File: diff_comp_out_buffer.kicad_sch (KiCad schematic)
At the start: 7 parts, among them U1 TLV3601, U48 SN74LVC2G126

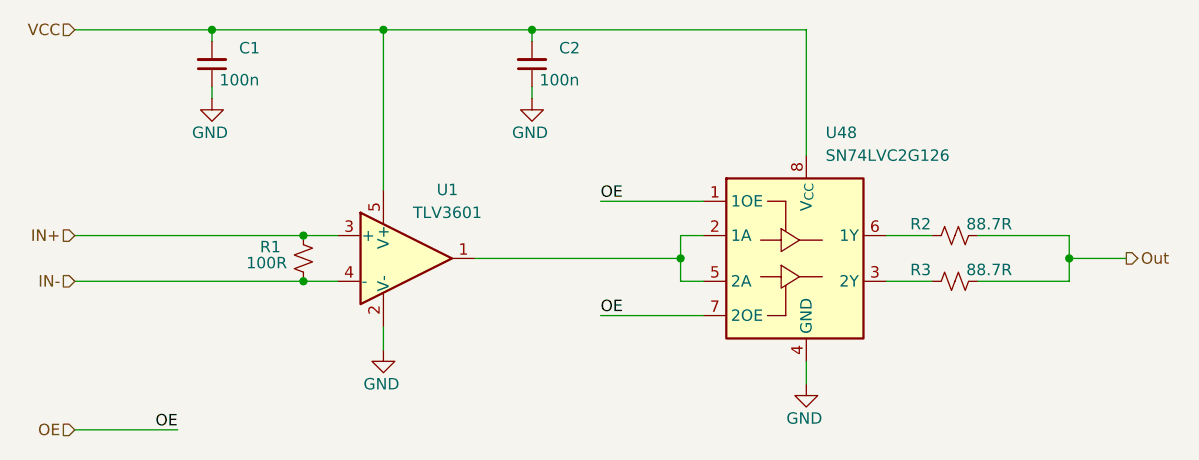
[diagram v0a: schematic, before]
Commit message: Fixed Silkscreen and BOM
All DRC/ERC errors are resolved.
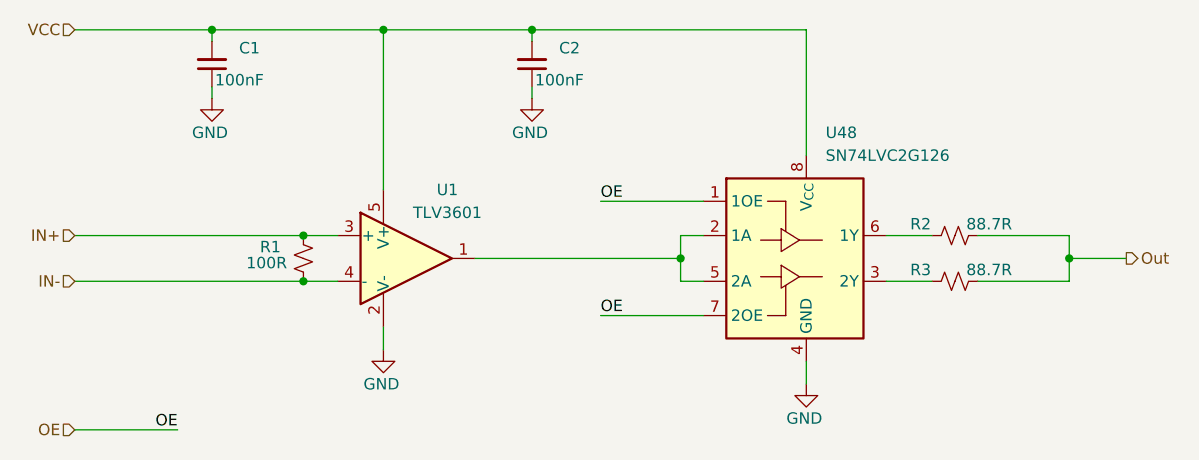
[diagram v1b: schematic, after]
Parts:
- C1, C2: value 100n -> 100nF; Digikey 1276-1935-2-ND -> 490-8020-6-ND; MPN CL10B104KB8NNWC -> GCM188R71H104KA57J; Manufacturer Samsung -> Murata
- R1: Digikey (none) -> 311-100LRDKR-ND
- R2, R3: Digikey (none) -> 541-88.7CDKR-ND
- U1: Digikey (none) -> 296-TLV3601DBVRDKR-ND; MPN (none) -> TLV3601DBVR; Manufacturer (none) -> Texas Instruments
- U48: Digikey (none) -> 296-32321-6-ND; MPN (none) -> SN74LVC2G126DCUT; Manufacturer (none) -> Texas Instruments
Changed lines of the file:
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@@
 			)
 		)
-		(property "Datasheet" "~"
+		(property "Datasheet" "https://www.ti.com/lit/ds/symlink/sn74lvc2g126.pdf"
 			(at 171.45 102.87 0)
 			(effects
@@
 			)
 		)
-		(property "Description" "Dual Bus Buffer Gate"
+		(property "Description" "IC BUFF 1.65V 8-VSSOP"
+			(at 171.45 102.87 0)
+			(effects
+				(font
+					(size 1.27 1.27)
+				)
+				(hide yes)
+			)
+		)
+		(property "Digikey" "296-32321-6-ND"
+			(at 171.45 102.87 0)
+			(effects
+				(font
+					(size 1.27 1.27)
+				)
+				(hide yes)
+			)
+		)
+		(property "MPN" "SN74LVC2G126DCUT"
+			(at 171.45 102.87 0)
+			(effects
+				(font
+					(size 1.27 1.27)
+				)
+				(hide yes)
+			)
+		)
+		(property "Manufacturer" "Texas Instruments"
 			(at 171.45 102.87 0)
 			(effects
@@
 			)
 		)
-		(property "Value" "100n"
+		(property "Value" "100nF"
 			(at 109.728 83.058 0)
 			(effects
@@
 			)
 		)
-		(property "Description" "Unpolarized capacitor, small symbol"
+		(property "Description" "CAP CER 0.1UF 50V X7R 0603"
 			(at 106.68 81.28 0)
 			(effects
@@
 			)
 		)
-		(property "Digikey" "1276-1935-2-ND"
+		(property "Digikey" "490-8020-6-ND"
 			(at 106.68 81.28 90)
 			(effects
@@
 			)
 		)
-		(property "MPN" "CL10B104KB8NNWC"
+		(property "MPN" "GCM188R71H104KA57J"
 			(at 106.68 81.28 90)
 			(effects
@@
 			)
 		)
-		(property "Manufacturer" "Samsung"
+		(property "Manufacturer" "Murata"
 			(at 106.68 81.28 90)
 			(effects
@@
 			)
 		)
-		(property "Datasheet" ""
+		(property "Datasheet" "https://www.ti.com/lit/ds/symlink/tlv3601.pdf"
 			(at 128.27 97.79 0)
 			(effects
@@
 			)
 		)
-		(property "Description" ""
+		(property "Description" "IC COMPARATOR 1CH SOT-23-5"
+			(at 128.27 102.87 0)
+			(effects
+				(font
+					(size 1.27 1.27)
+				)
+				(hide yes)
+			)
+		)
+		(property "Digikey" "296-TLV3601DBVRDKR-ND"
+			(at 128.27 102.87 0)
+			(effects
+				(font
+					(size 1.27 1.27)
+				)
+				(hide yes)
+			)
+		)
+		(property "MPN" "TLV3601DBVR"
+			(at 128.27 102.87 0)
+			(effects
+				(font
+					(size 1.27 1.27)
+				)
+				(hide yes)
+			)
+		)
+		(property "Manufacturer" "Texas Instruments"
 			(at 128.27 102.87 0)
 			(effects
@@
 			)
 		)
+		(property "Digikey" "311-100LRDKR-ND"
+			(at 116.84 102.87 0)
+			(effects
+				(font
+					(size 1.27 1.27)
+				)
+				(hide yes)
+			)
+		)
 		(pin "1"
 		)
@@
 			)
 		)
-		(property "Description" "RES SMD 88.7 OHM 1% 1/4W 0805"
+		(property "Description" "RES SMD 88.7 OHM 1% 1/8W 0805"
 			(at 189.23 105.41 0)
 			(effects
@@
 		(property "Manufacturer" "Vishay Dale"
 			(at 189.23 105.41 0)
+			(effects
+				(font
+					(size 1.27 1.27)
+				)
+				(hide yes)
+			)
+		)
+		(property "Digikey" "541-88.7CDKR-ND"
+			(at 189.23 105.41 90)
 			(effects
 				(font
@@
 			)
 		)
-		(property "Value" "100n"
+		(property "Value" "100nF"
 			(at 145.288 83.058 0)
 			(effects
@@
 			)
 		)
-		(property "Description" "Unpolarized capacitor, small symbol"
+		(property "Description" "CAP CER 0.1UF 50V X7R 0603"
 			(at 142.24 81.28 0)
 			(effects
@@
 			)
 		)
-		(property "Digikey" "1276-1935-2-ND"
+		(property "Digikey" "490-8020-6-ND"
 			(at 142.24 81.28 90)
 			(effects
@@
 			)
 		)
-		(property "MPN" "CL10B104KB8NNWC"
+		(property "MPN" "GCM188R71H104KA57J"
 			(at 142.24 81.28 90)
 			(effects
@@
 			)
 		)
-		(property "Manufacturer" "Samsung"
+		(property "Manufacturer" "Murata"
 			(at 142.24 81.28 90)
 			(effects
@@
 			)
 		)
-		(property "Description" "RES SMD 88.7 OHM 1% 1/4W 0805"
+		(property "Description" "RES SMD 88.7 OHM 1% 1/8W 0805"
 			(at 189.23 100.33 0)
 			(effects
@@
 			(effects
 				(font
+					(size 1.27 1.27)
+				)
+				(hide yes)
+			)
+		)
+		(property "Digikey" "541-88.7CDKR-ND"
+			(at 189.23 100.33 90)
+			(effects
+				(font

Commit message: Final Draft for project
- Changed LDO for Digital Output driver to a LP3855-ADJ
- Aligned Digital Output driver sections
- Added Additional Capacitance on each digital output drive channel
- Revised Differential Lines geometry on top layer
- Revised Power routing and internal planes
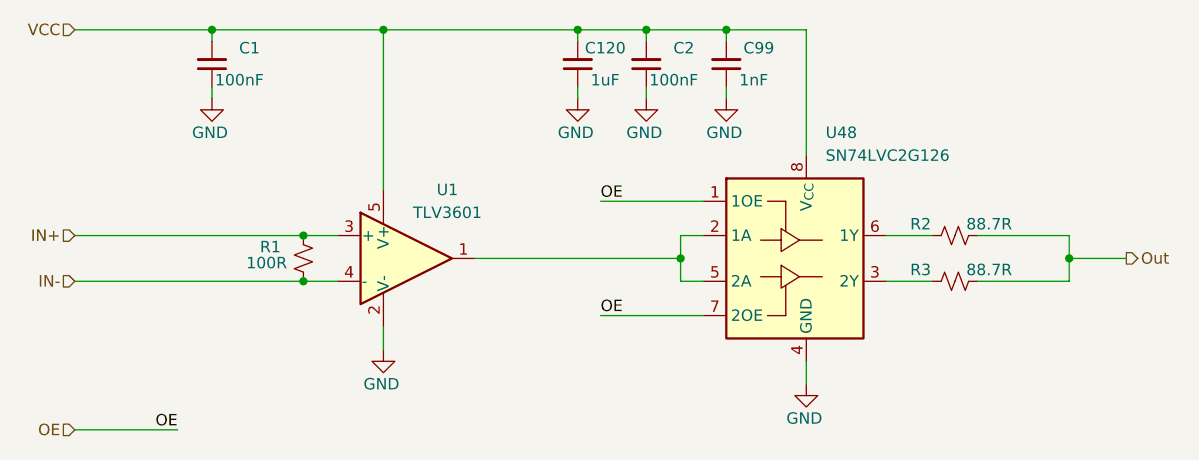
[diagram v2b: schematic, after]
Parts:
- added C120: 1uF, Capacitor_SMD:C_0603_1608Metric, symbol Device:C_Small
- added C99: 1nF, Capacitor_SMD:C_0603_1608Metric, symbol Device:C_Small
- C1, C2: Digikey 490-8020-6-ND -> (none)
- R1: Digikey 311-100LRDKR-ND -> (none)
- R2, R3: Digikey 541-88.7CDKR-ND -> (none)
- U1: Digikey 296-TLV3601DBVRDKR-ND -> (none)
- U48: Digikey 296-32321-6-ND -> (none)
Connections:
- net GND: now also C120.1, C99.1
- net VCC: now also C120.2, C99.2
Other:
- moved on the sheet: C2

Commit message: Updated Layout of XOs and Digital Output Sections
- Added some additional comments to schematics (Y1&Y2)
- Added additional ground vias around U44
- Add GND planes around 1.8V LDOs (U21&U28)
- Straightened out some power routing tracks with 90deg bends
- Revised routing of Y1&Y2
- Revised routing of each digital output section
- All DCR/ERC errors resolved.
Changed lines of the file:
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@@
+	)
+	(junction
+		(at 146.05 109.22)
+		(diameter 0)
+		(color 0 0 0 0)
 	)
 	(junction
@@
 	(wire
 		(pts
-			(xy 161.29 109.22) (xy 149.86 109.22)
-		)
-		(stroke
-			(width 0)
-			(type default)
-		)
-	)
-	(wire
-		(pts
 			(xy 191.77 105.41) (xy 201.93 105.41)
 		)
@@
 	(wire
 		(pts
+			(xy 146.05 96.52) (xy 161.29 96.52)
+		)
+		(stroke
+			(width 0)
+			(type default)
+		)
+	)
+	(wire
+		(pts
 			(xy 163.83 77.47) (xy 154.94 77.47)
 		)
@@
 	(wire
 		(pts
-			(xy 161.29 96.52) (xy 149.86 96.52)
-		)
-		(stroke
-			(width 0)
-			(type default)
-		)
-	)
-	(wire
-		(pts
 			(xy 161.29 105.41) (xy 158.75 105.41)
 		)
@@
 	(wire
 		(pts
+			(xy 146.05 109.22) (xy 161.29 109.22)
+		)
+		(stroke
+			(width 0)
+			(type default)
+		)
+	)
+	(wire
+		(pts
 			(xy 172.72 91.44) (xy 172.72 77.47)
 		)
@@
 	(wire
 		(pts
-			(xy 91.44 121.92) (xy 102.87 121.92)
+			(xy 91.44 121.92) (xy 146.05 121.92)
 		)
 		(stroke
@@
 	(wire
 		(pts
+			(xy 146.05 109.22) (xy 146.05 96.52)
+		)
+		(stroke
+			(width 0)
+			(type default)
+		)
+	)
+	(wire
+		(pts
+			(xy 146.05 121.92) (xy 146.05 109.22)
+		)
+		(stroke
+			(width 0)
+			(type default)
+		)
+	)
+	(wire
+		(pts
 			(xy 91.44 100.33) (xy 116.84 100.33)
 		)
@@
 		)
 	)
-	(label "OE"
-		(at 149.86 96.52 0)
-		(effects
-			(font
-				(size 1.27 1.27)
-			)
-			(justify left bottom)
-		)
-	)
-	(label "OE"
-		(at 149.86 109.22 0)
-		(effects
-			(font
-				(size 1.27 1.27)
-			)
-			(justify left bottom)
-		)
-	)
-	(label "OE"
-		(at 102.87 121.92 180)
-		(effects
-			(font
-				(size 1.27 1.27)
-			)
-			(justify right bottom)
-		)
-	)

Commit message: Updates after external review
- Changed Value of R66 & R67
- Added 100nF cap (C104) at input of U22
- Added GND via in center of U24 (like other LDO's)
- Changed 1nF Caps in Digital output section to 10nF
- Rounded pads of (T1-T4)
- Adjusted traces between T1-T4 and their respective MMCX connector
- Added FB1 & C136 at output of U22(5.45V switcher)
- Exchanged R88(0ohm) for a Ferrite Bead at input to U22(5.45V switcher)
- Revised layout of U22 area to more closely follow the data sheet.
- Exchanged R73&R42 at input to U44 for a ferrite bead (FB3)
- Exchanged R86/87/98/99 at input of TLV757 LDO for ferrite beads
- Added 1uF caps to VDD, VDDA, and VDDS power rails on Jitter Cleaner
- Changed C46,C47,C75,C77 from 1uF to 10uF caps
- Added Ferrite and 2 caps for each VDDO power rail on the jitter cleaners
- Adjusted layout around pint 26,27,28, of U18
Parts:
- C99: value 1nF -> 10nF; MPN GCM188R71H102KA37D -> GRM1885C1H103JA01D
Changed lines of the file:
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@@
 			)
 		)
-		(property "Value" "1nF"
+		(property "Value" "10nF"
 			(at 166.878 83.058 0)
 			(effects
@@
 			)
 		)
-		(property "Description" "CAP CER 1000PF 50V X7R 0603"
+		(property "Description" "CAP CER 10000PF 50V C0G/NP0 0603"
 			(at 163.83 81.28 0)
 			(effects
@@
 			)
 		)
-		(property "MPN" "GCM188R71H102KA37D"
+		(property "MPN" "GRM1885C1H103JA01D"
 			(at 163.83 81.28 90)
 			(effects
